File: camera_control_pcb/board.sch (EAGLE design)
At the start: 20 parts, among them Q1 MPSA42

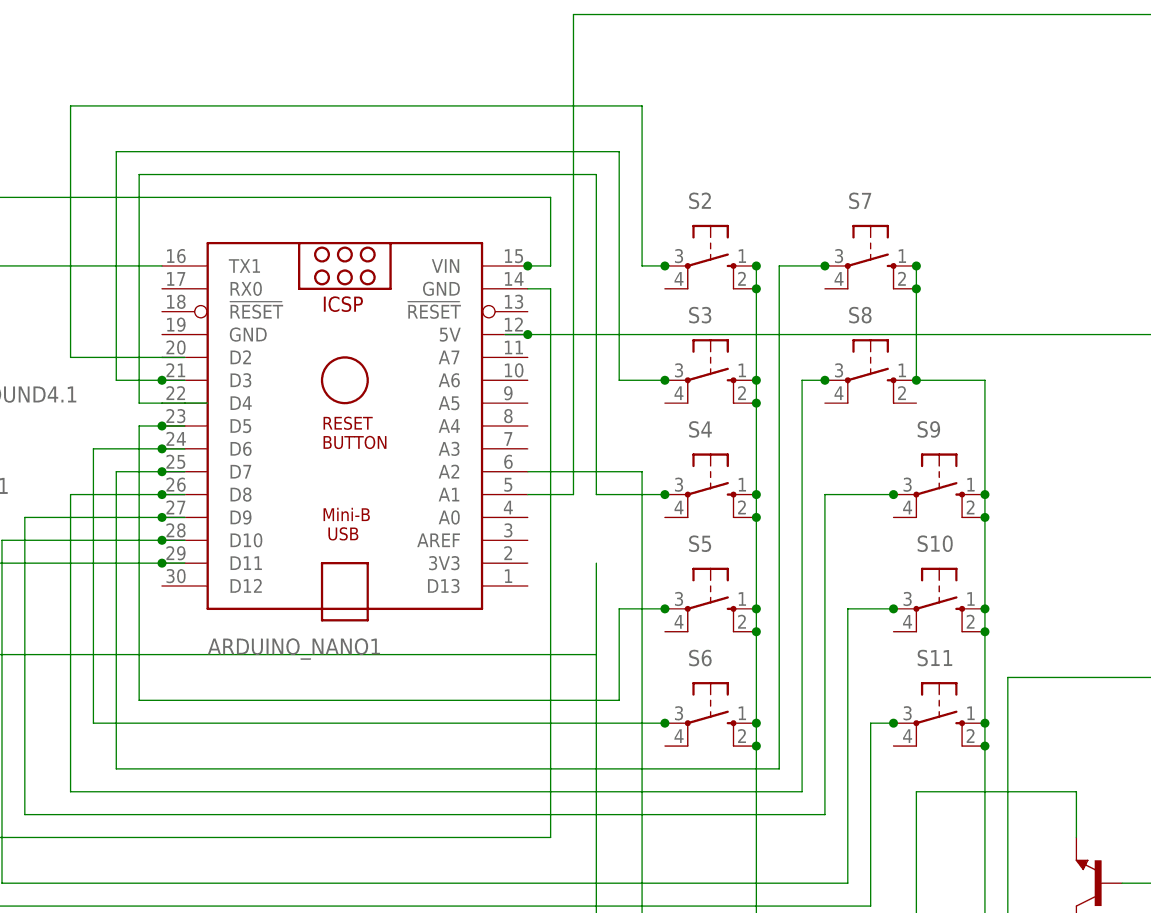
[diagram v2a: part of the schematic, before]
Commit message: Fix switch sizes to 10mm
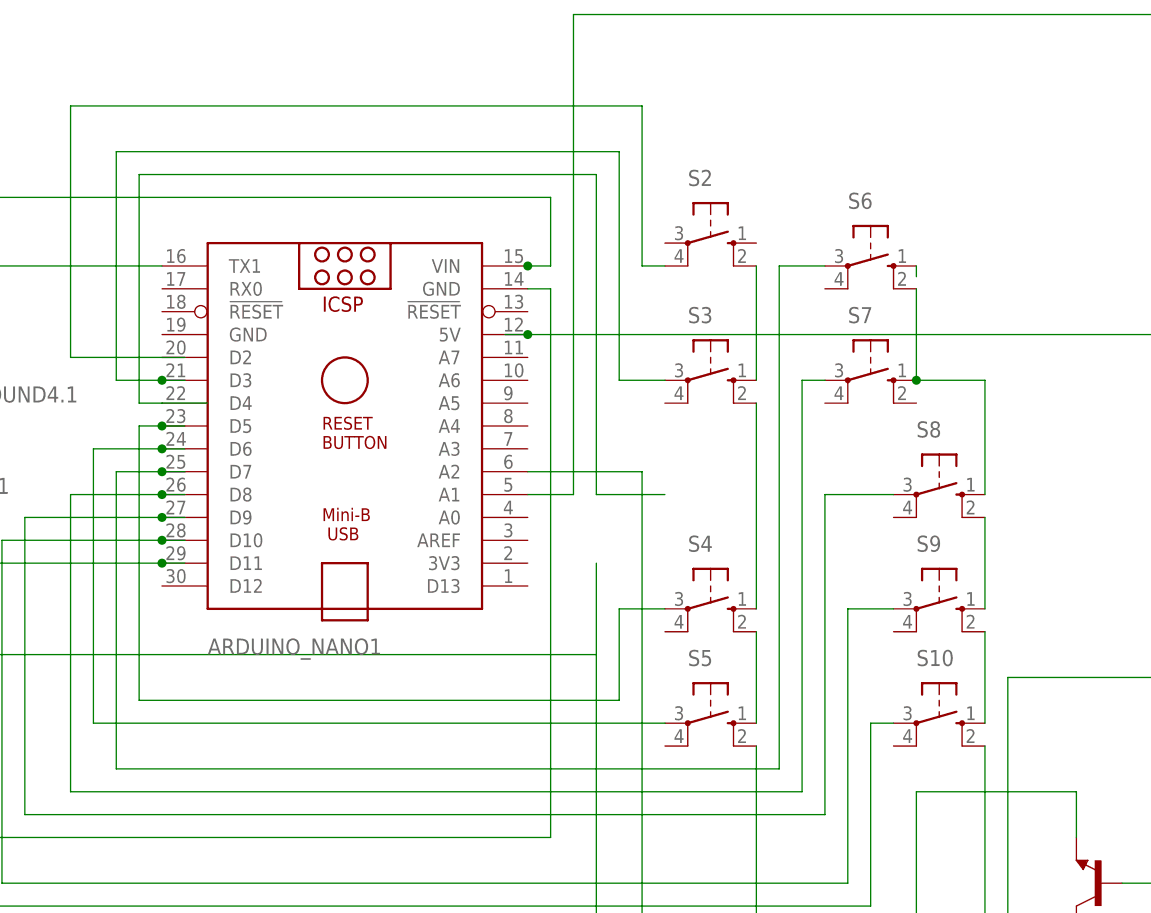
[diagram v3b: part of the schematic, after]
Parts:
- removed S11: (no value), switch-omron:40-XX
- S10, S2, S3, S4, S5, S6, S7, S8, S9: device switch-omron:40-XX -> switch-omron:10-XX
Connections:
- new net N$20: S2.S1, S3.S
- new net N$21: S3.S1, S4.S
- new net N$22: S4.S1, S5.S
- new net N$23: S6.S
- new net N$24: S6.S1, S7.S, S8.S
- new net N$25: S8.S1, S9.S
- new net N$26: S10.S, S9.S1
- net N$10: now also S8.P; no longer S9.P
- net N$11: now also S9.P; no longer S10.P
- net N$12: now also S10.P; no longer S11.P
- net N$13: now also S2.P1; no longer S2.P
- net N$14: no longer S4.P
- net N$3: no longer S10.S, S11.S, S11.S1, S2.S, S2.S1, S3.S, S3.S1, S4.S, S4.S1, S5.S, S6.S, S6.S1, S7.S, S7.S1, S8.S, S9.S, S9.S1
- net N$6: now also S6.P; no longer S7.P
- net N$7: now also S4.P; no longer S5.P
- net N$8: now also S5.P; no longer S6.P
- net N$9: now also S7.P; no longer S8.P
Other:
- moved on the sheet: S10, S2, S4, S5, S6, S7, S8, S9

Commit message: Example Board Layout with 11 vias
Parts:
- added LED1: (no value), led:LED5MM
- added S11: (no value), switch-omron:10-XX
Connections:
- new net N$27: S11.S1, S4.S
- new net N$28: ARDUINO_NANO1.D13, LED1.A
- net N$14: now also S11.P
- net N$21: now also S11.S; no longer S4.S
- net N$3: now also LED1.C
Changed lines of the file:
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@@
 <part name="S9" library="switch-omron" library_urn="urn:adsk.eagle:library:377" deviceset="10-XX" device="" package3d_urn="urn:adsk.eagle:package:27496/1"/>
 <part name="S10" library="switch-omron" library_urn="urn:adsk.eagle:library:377" deviceset="10-XX" device="" package3d_urn="urn:adsk.eagle:package:27496/1"/>
+<part name="S11" library="switch-omron" library_urn="urn:adsk.eagle:library:377" deviceset="10-XX" device="" package3d_urn="urn:adsk.eagle:package:27496/1"/>
+<part name="LED1" library="led" library_urn="urn:adsk.eagle:library:259" deviceset="LED" device="5MM" package3d_urn="urn:adsk.eagle:package:15799/2"/>
 </parts>
 <sheets>
@@
 <attribute name="NAME" x="106.68" y="36.83" size="1.778" layer="95"/>
 <attribute name="VALUE" x="112.395" y="34.29" size="1.778" layer="96"/>
+</instance>
+<instance part="S11" gate="1" x="83.82" y="55.88" smashed="yes" rot="R270">
+<attribute name="NAME" x="81.28" y="62.23" size="1.778" layer="95"/>
+<attribute name="VALUE" x="86.995" y="59.69" size="1.778" layer="96"/>
+</instance>
+<instance part="LED1" gate="G$1" x="66.04" y="-35.56" smashed="yes">
+<attribute name="NAME" x="69.596" y="-40.132" size="1.778" layer="95" rot="R90"/>
+<attribute name="VALUE" x="71.755" y="-40.132" size="1.778" layer="96" rot="R90"/>
 </instance>
 </instances>
@@
 <wire x1="114.3" y1="27.94" x2="114.3" y2="-12.7" width="0.1524" layer="91"/>
 <pinref part="S10" gate="1" pin="S1"/>
+<pinref part="LED1" gate="G$1" pin="C"/>
+<wire x1="66.04" y1="-40.64" x2="-17.78" y2="-40.64" width="0.1524" layer="91"/>
+<wire x1="-17.78" y1="-40.64" x2="-17.78" y2="-12.7" width="0.1524" layer="91"/>
+<junction x="-17.78" y="-12.7"/>
 </segment>
 </net>
@@
 <wire x1="22.86" y1="66.04" x2="27.94" y2="66.04" width="0.1524" layer="91"/>
 <wire x1="20.32" y1="66.04" x2="22.86" y2="66.04" width="0.1524" layer="91"/>
+<pinref part="S11" gate="1" pin="P"/>
 </segment>
 </net>
 <net name="N$15" class="0">
 <segment>
-<wire x1="71.12" y1="48.26" x2="71.12" y2="38.1" width="0.1524" layer="91"/>
 <wire x1="71.12" y1="38.1" x2="71.12" y2="-5.08" width="0.1524" layer="91"/>
 <wire x1="71.12" y1="-5.08" x2="116.84" y2="-5.08" width="0.1524" layer="91"/>
@@
 <segment>
 <pinref part="S3" gate="1" pin="S1"/>
-<wire x1="88.9" y1="66.04" x2="88.9" y2="43.18" width="0.1524" layer="91"/>
-<pinref part="S4" gate="1" pin="S"/>
+<wire x1="88.9" y1="66.04" x2="88.9" y2="55.88" width="0.1524" layer="91"/>
+<pinref part="S11" gate="1" pin="S"/>
 </segment>
 </net>
@@
 </segment>
 </net>
+<net name="N$27" class="0">
+<segment>
+<pinref part="S4" gate="1" pin="S"/>
+<wire x1="88.9" y1="53.34" x2="88.9" y2="43.18" width="0.1524" layer="91"/>
+<pinref part="S11" gate="1" pin="S1"/>
+</segment>
+</net>
+<net name="N$28" class="0">
+<segment>
+<pinref part="ARDUINO_NANO1" gate="G$1" pin="D13"/>
+<wire x1="63.5" y1="45.72" x2="63.5" y2="-33.02" width="0.1524" layer="91"/>
+<pinref part="LED1" gate="G$1" pin="A"/>
+<wire x1="63.5" y1="-33.02" x2="66.04" y2="-33.02" width="0.1524" layer="91"/>
+</segment>
+</net>
